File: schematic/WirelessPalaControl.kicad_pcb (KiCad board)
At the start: 2 copper layers, 25.4 x 33.7 mm, 20 parts, among them J1 6P6C, J2 MCU UART, Q1 BC847B, Q2 BC847B, U1 SI8621, U2 WeMos_mini

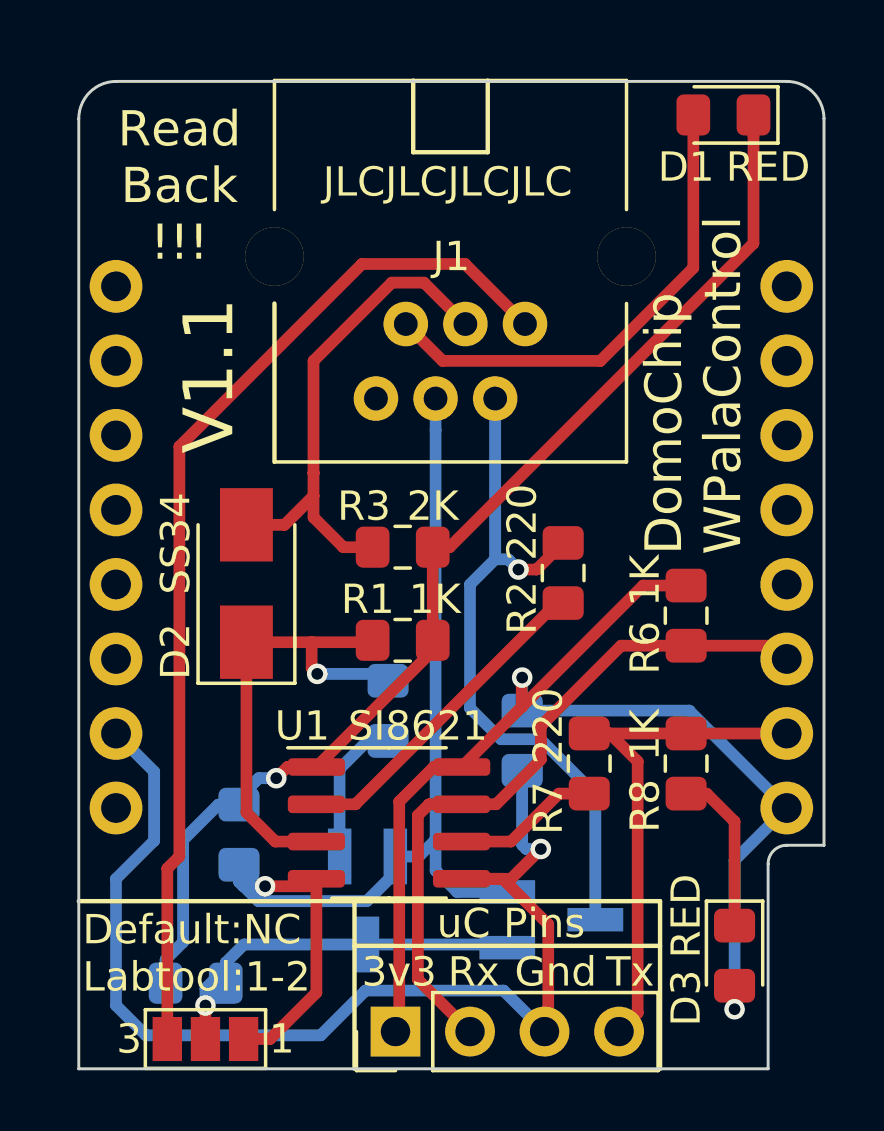
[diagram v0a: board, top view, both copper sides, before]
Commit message: New Hardware Version (V2.0) (#65)
* Add hw version detection

* New PCB version

* Implement Hardware detection

* Do Not Place J2

* New box

* Update box

* Update box img

* Update schematic

* Update pcb img

* Update cabling img

* Update BUILD.md

* Update cabling part in README.md

* Change R4 to 2K

* Update schematic and botoom pcb

* Slightly adjust box
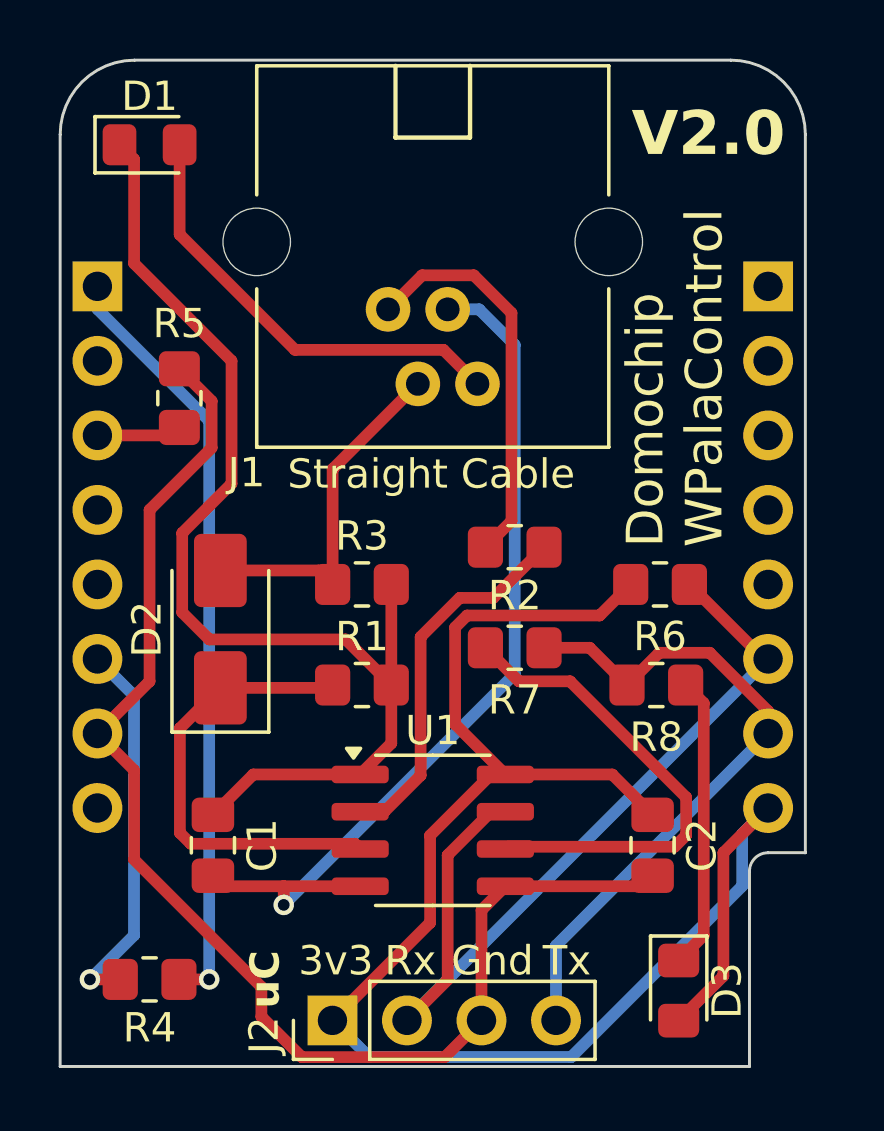
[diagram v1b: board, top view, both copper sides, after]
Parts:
- removed JP1: SldJmp_3_Open, Jumper:SolderJumper-3_P1.3mm_Open_Pad1.0x1.5mm_NumberLabels
- removed Q1, Q2: BC847B, Package_TO_SOT_SMD:SOT-23_Handsoldering
- removed U2: WeMos_mini, wemos_d1_mini:wemos-d1-mini-DIL-only
- added J3: WeMos_mini_Hat_Left, wemos_d1_mini:WeMos_D1_mini_Hat_Left, B.Cu at (24.1, 31.8)
- added J4: WeMos_mini_Hat_Right, wemos_d1_mini:WeMos_D1_mini_Hat_Right, B.Cu at (47.0, 31.8)
- C1, C2: footprint Capacitor_SMD:C_0805_2012Metric_Pad1.15x1.40mm_HandSolder -> Capacitor_SMD:C_0805_2012Metric_Pad1.18x1.45mm_HandSolder; moved to F.Cu
- J1: value 6P6C -> 6P4C; footprint MyRJ:Ali_RJ12 -> MyRJ:Ali_RJ11
- R1, R2, R3, R6, R7: footprint Resistor_SMD:R_0805_2012Metric_Pad1.15x1.40mm_HandSolder -> Resistor_SMD:R_0805_2012Metric_Pad1.20x1.40mm_HandSolder
- R4: footprint Resistor_SMD:R_0805_2012Metric_Pad1.15x1.40mm_HandSolder -> Resistor_SMD:R_0805_2012Metric_Pad1.20x1.40mm_HandSolder; moved to F.Cu
- R5: value 2K -> 10K; footprint Resistor_SMD:R_0805_2012Metric_Pad1.15x1.40mm_HandSolder -> Resistor_SMD:R_0805_2012Metric_Pad1.20x1.40mm_HandSolder; moved to F.Cu
- R8: value 1K -> 2K; footprint Resistor_SMD:R_0805_2012Metric_Pad1.15x1.40mm_HandSolder -> Resistor_SMD:R_0805_2012Metric_Pad1.20x1.40mm_HandSolder
- moved R5 19.9 mm to (26.9, 35.6), turned to 90 degrees
- moved D1 19.6 mm to (25.9, 26.9), turned to 0 degrees
- moved R4 12.2 mm to (25.9, 55.4), turned to 180 degrees
- moved C2 5.70 mm to (43.1, 50.8)
- moved R7 4.69 mm to (38.4, 44.1), turned to 180 degrees
- moved R8 2.86 mm to (43.2, 45.3), turned to 0 degrees
- moved J1 2.79 mm to (34.0, 32.5)
- moved D3 2.25 mm to (43.9, 55.8)
- moved J2 2.18 mm to (32.1, 56.8)
- moved R1 2.06 mm to (33.1, 45.3)
- moved R3 1.88 mm to (33.1, 41.9)
- moved R2 1.87 mm to (38.4, 40.6), turned to 0 degrees
- moved D2 1.79 mm to (28.3, 43.4)
- moved U1 1.51 mm to (35.6, 50.3)
- moved R6 1.39 mm to (43.3, 41.9), turned to 180 degrees
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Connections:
- net /GND1 renamed GND1
- net /RXuC renamed RXuC
- net /TXuC renamed TXuC
- net /VDD2 renamed VDD2
- C1 pad 1: /VDD1 -> VDD1
- C2 pad 2: /GND2 -> GND2
- D1 pad 1: /VDD1 -> VDD1
- D1 pad 2: Net-(D1-Pad2) -> Net-(D1-A)
- D2 pad 1: Net-(D2-Pad1) -> Net-(D2-K)
- J1 pad 1: (no net) -> /Tx
- J1 pad 2: Net-(D1-Pad2) -> /Rx
- J1 pad 4: /Rx -> Net-(D1-A)
- J2 pad 3: /GND2 -> GND2
- R1 pad 1: Net-(D2-Pad1) -> Net-(D2-K)
- R1 pad 2: /VDD1 -> VDD1
- R2 pad 1: /Tx-RxH -> /Tx
- R3 pad 2: /VDD1 -> VDD1
- R4 pad 1: Net-(D2-Pad1) -> Net-(J3-Tx)
- R5 pad 1: /VDD1 -> Net-(J3-D1)
- R5 pad 2: /Q2B -> GND2
- U1 pad 1: /VDD1 -> VDD1
- U1 pad 3: Net-(D2-Pad1) -> Net-(D2-K)
- U1 pad 5: /GND2 -> GND2
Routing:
- net GND2: track 0.00 -> 45.1 mm
- net /GND2: track 40.3 -> 0.00 mm, vias 1 -> 0
- net /VDD1: track 39.1 -> 0.00 mm, vias 1 -> 0
- net VDD1: track 0.00 -> 38.9 mm
- net Net-(J1-Pad6): track 35.6 -> 0.00 mm
- net Net-(J3-Tx): track 0.00 -> 26.2 mm, vias 0 -> 1
- net /Tx-RxH: track 23.5 -> 0.00 mm, vias 1 -> 0
- net Net-(D1-Pad2): track 16.8 -> 0.00 mm
- net Net-(D2-Pad1): track 16.4 -> 0.00 mm, vias 1 -> 0
- net Net-(D2-K): track 0.00 -> 15.7 mm
- net Net-(D1-A): track 0.00 -> 15.3 mm
- net VDD2: track 42.3 -> 57.4 mm, vias 2 -> 0
- net /Tx: track 0.00 -> 13.6 mm
- net /Q2B: track 13.3 -> 0.00 mm, vias 1 -> 0
- net Net-(U1-B2): track 5.03 -> 16.6 mm
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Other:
- board size 25.4 x 33.7 mm -> 25.4 x 34.3 mm
- board text added: "C1,C2: 100n D1,D3: Red Led D2: SS34 R1,R6: 1K R2,R7: 220 R3,R4,R8: 2K R5: 10K U1: Si8621"
- board text added: "Domochip WPalaControl"
- board text added: "Domochip WPalaControl V2.0"
- board text added: "Straight Cable"
- board text added: "Use RJ11 straight cable"
- board text added: "V2.0"
- board text added: "uC"
- board text removed: "!!!"
- board text removed: "1"
- board text removed: "9"
- board text removed: "Default:NC Labtool:1-2"
- board text removed: "DomoChip WPalaControl"
- board text removed: "DomoChip WPalaControl V1.1"
- board text removed: "Read Back !!!"
- board text removed: "Use RJ11 cross cable (phone standard)"
- board text removed: "V1.1"
- board text removed: "uC Pins"
